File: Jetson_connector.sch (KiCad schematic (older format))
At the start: 18 parts, among them IC2 AT24MAC402-MAHM-T, J2 QTH-060-01-L-D-A, U1 LP5907MFX-1.8

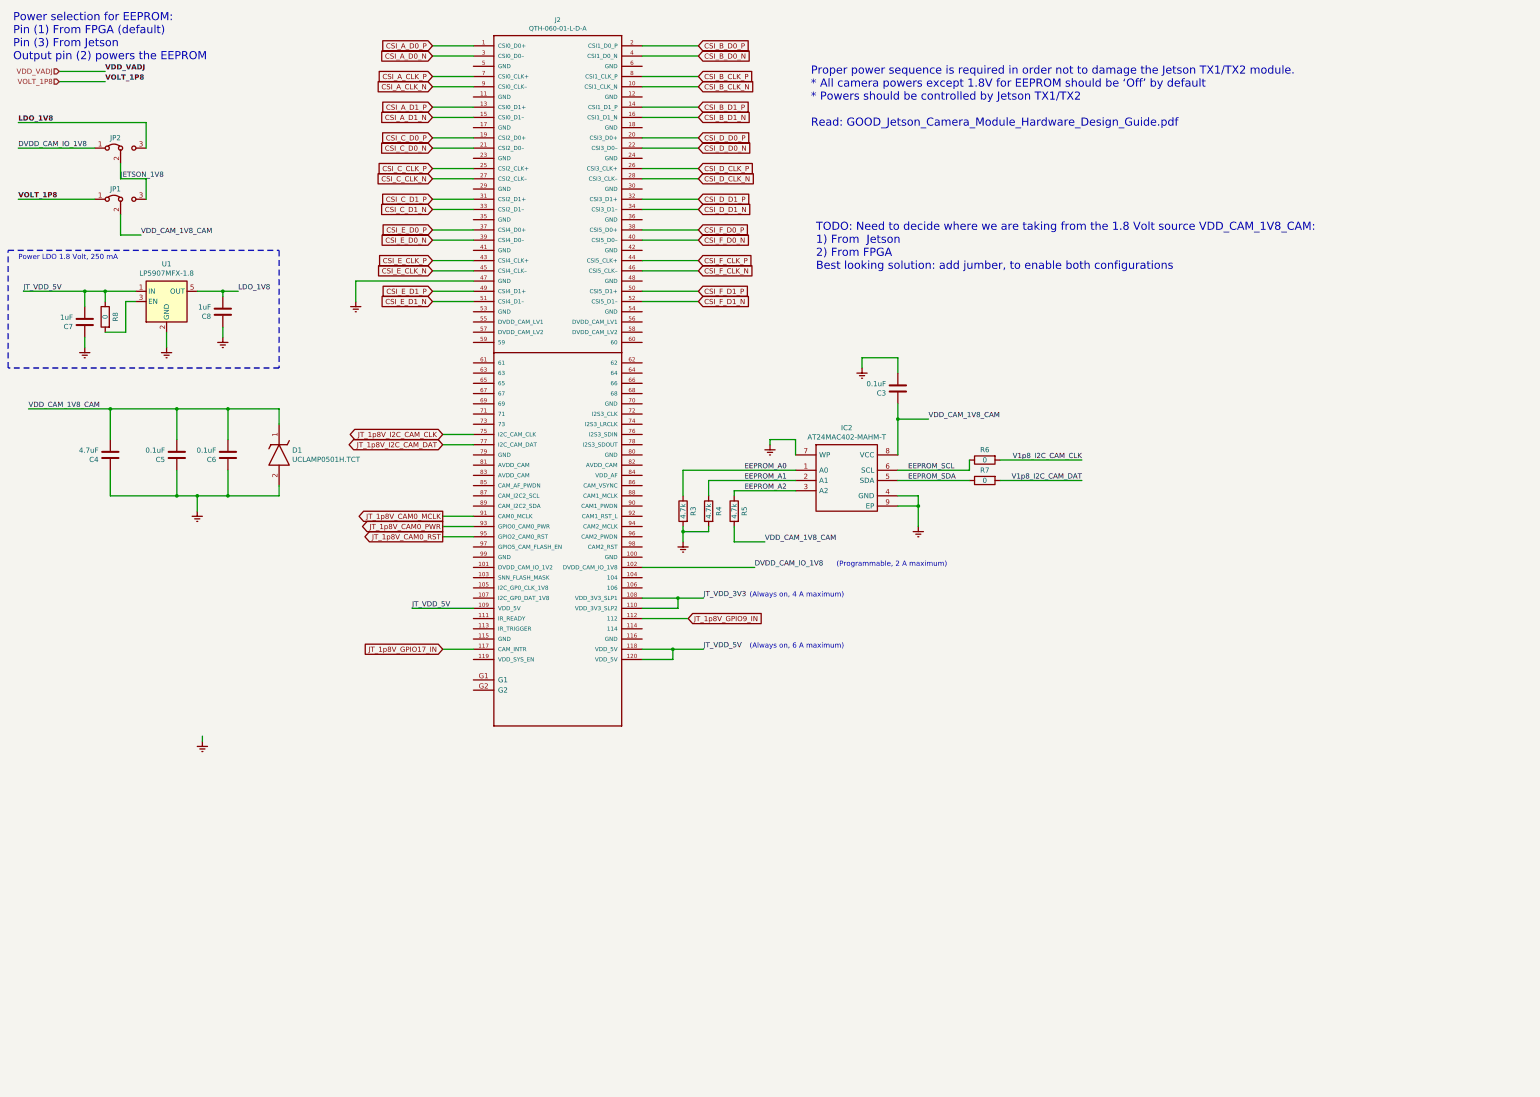
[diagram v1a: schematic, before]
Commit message: adding more power supplies
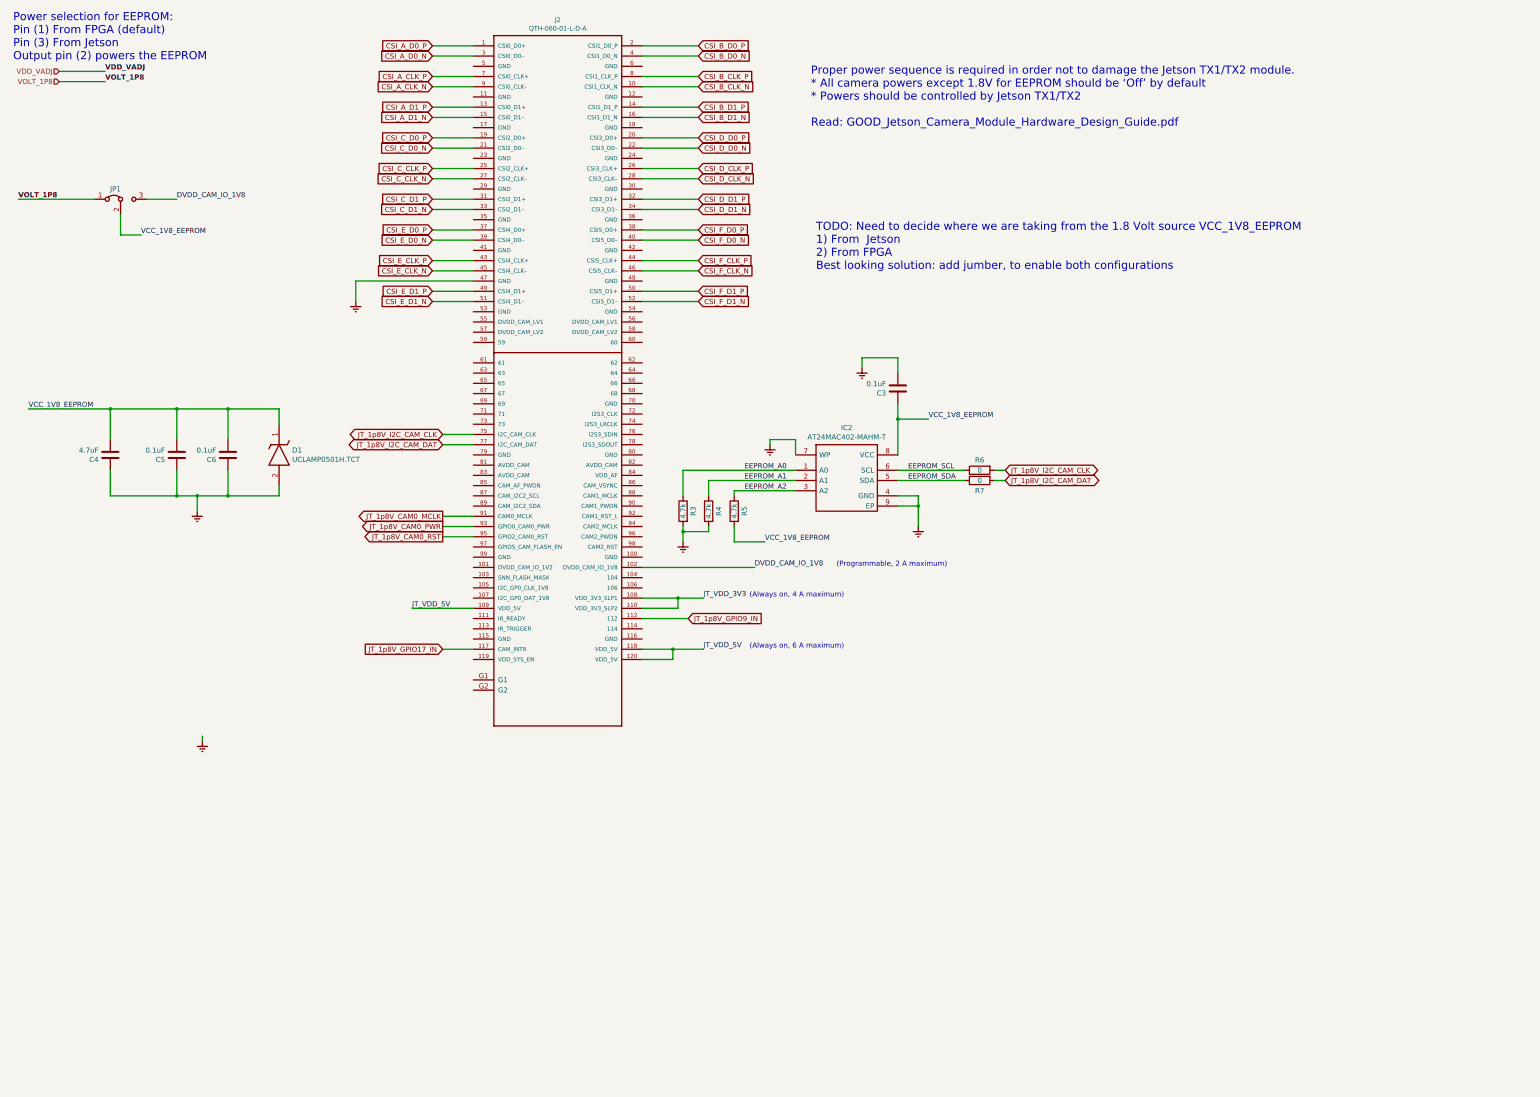
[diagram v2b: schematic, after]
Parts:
- removed C7, C8: 1uF, Capacitors_SMD:C_0805, symbol FMC_MIPI_v2:C
- removed JP2: Jumper_3_Bridged12, Pin_Headers:Pin_Header_Straight_1x03_Pitch2.54mm, symbol Jumper:Jumper_3_Bridged12
- removed R8: 0, Resistors_SMD:R_0805, symbol Device:R
- removed U1: LP5907MFX-1.8, TO_SOT_Packages_SMD:SOT-23-5, symbol Regulator_Linear:LP5907MFX-1.8
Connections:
- net JETSON_1V8 is gone; now on net DVDD_CAM_IO_1V8: JP1.3 (B)
- net V1p8_I2C_CAM_CLK is gone; now on net JT_1p8V_I2C_CAM_CLK: R6.2
- net V1p8_I2C_CAM_DAT is gone; now on net JT_1p8V_I2C_CAM_DAT: R7.2
- net VDD_CAM_1V8_CAM renamed VCC_1V8_EEPROM
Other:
- note added: "TODO: Need to decide where we are taking from the 1.8 Volt source VCC_1V8_EEPROM\n1) From Jetson\n2) From FPGA\nBest looking solution: add jumber, to enable both configurations"
- note removed: "Power LDO 1.8 Volt, 250 mA"
- note removed: "TODO: Need to decide where we are taking from the 1.8 Volt source VDD_CAM_1V8_CAM:\n1) From Jetson\n2) From FPGA\nBest looking solution: add jumber, to enable both configurations"
- moved on the sheet: R6, R7

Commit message: cleanup 3D shapes
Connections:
- net DVDD_CAM_IO_1V8 renamed JT_VDD_1V8
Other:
- moved on the sheet: C3, IC2, R3, R4, R5, R6, R7

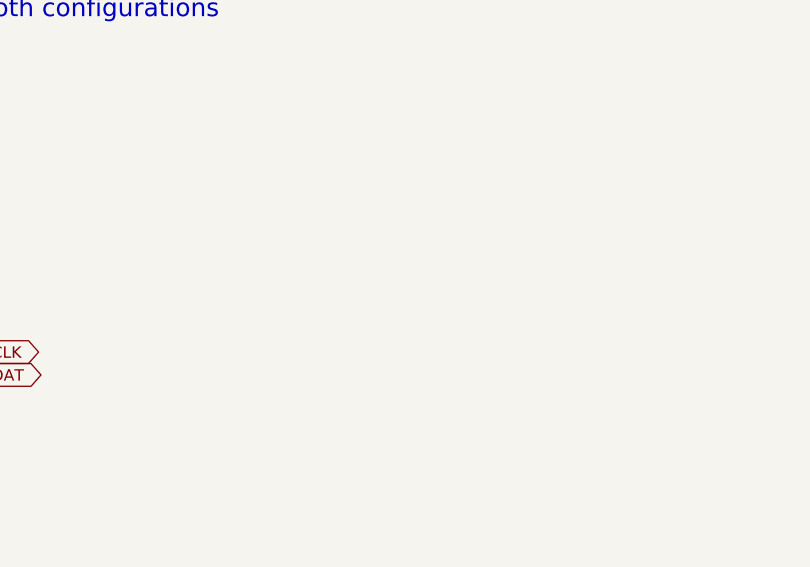
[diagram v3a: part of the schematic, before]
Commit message: Adding more LVDS lines
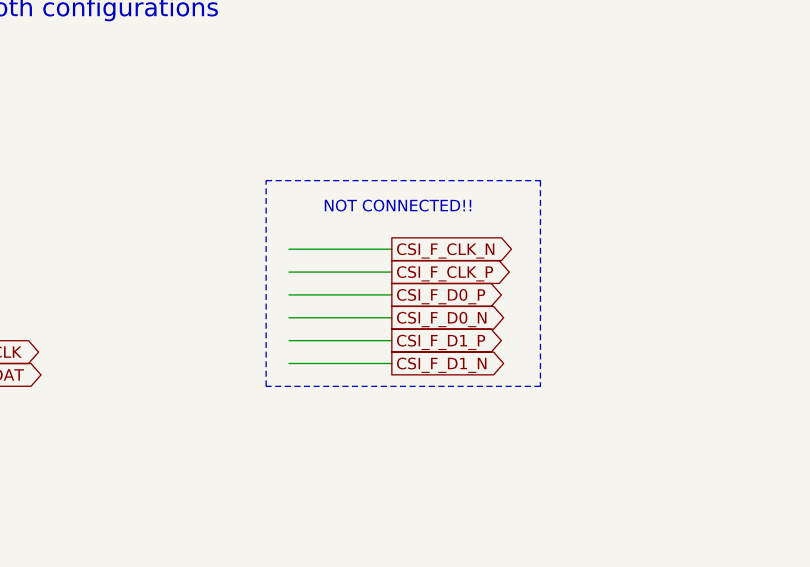
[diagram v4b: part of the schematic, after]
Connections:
- wire segments 108 -> 114
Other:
- note added: "NOT CONNECTED!!"
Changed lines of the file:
@@
 $Descr A4 11693 8268
 encoding utf-8
-Sheet 3 12
+Sheet 3 19
 Title ""
 Date ""
@@
 Text Label 7900 5200 0    50   ~ 0
 VCC_1V8_EEPROM
+Text GLabel 12700 4250 2    50   Output ~ 0
+CSI_F_D0_P
+Text GLabel 12700 4350 2    50   Output ~ 0
+CSI_F_D0_N
+Text GLabel 12700 4150 2    50   Output ~ 0
+CSI_F_CLK_P
+Text GLabel 12700 4050 2    50   Output ~ 0
+CSI_F_CLK_N
+Text GLabel 12700 4450 2    50   Output ~ 0
+CSI_F_D1_P
+Text GLabel 12700 4550 2    50   Output ~ 0
+CSI_F_D1_N
+Wire Wire Line
+	12250 4050 12700 4050
+Wire Wire Line
+	12250 4150 12700 4150
+Wire Wire Line
+	12250 4250 12700 4250
+Wire Wire Line
+	12250 4350 12700 4350
+Wire Wire Line
+	12250 4450 12700 4450
+Wire Wire Line
+	12250 4550 12700 4550
+Text Notes 12400 3900 0    50   ~ 0
+NOT CONNECTED!!
+Wire Notes Line
+	12150 3750 13350 3750
+Wire Notes Line
+	13350 3750 13350 4650
+Wire Notes Line
+	13350 4650 12150 4650
+Wire Notes Line
+	12150 4650 12150 3750
 $EndSCHEMATC

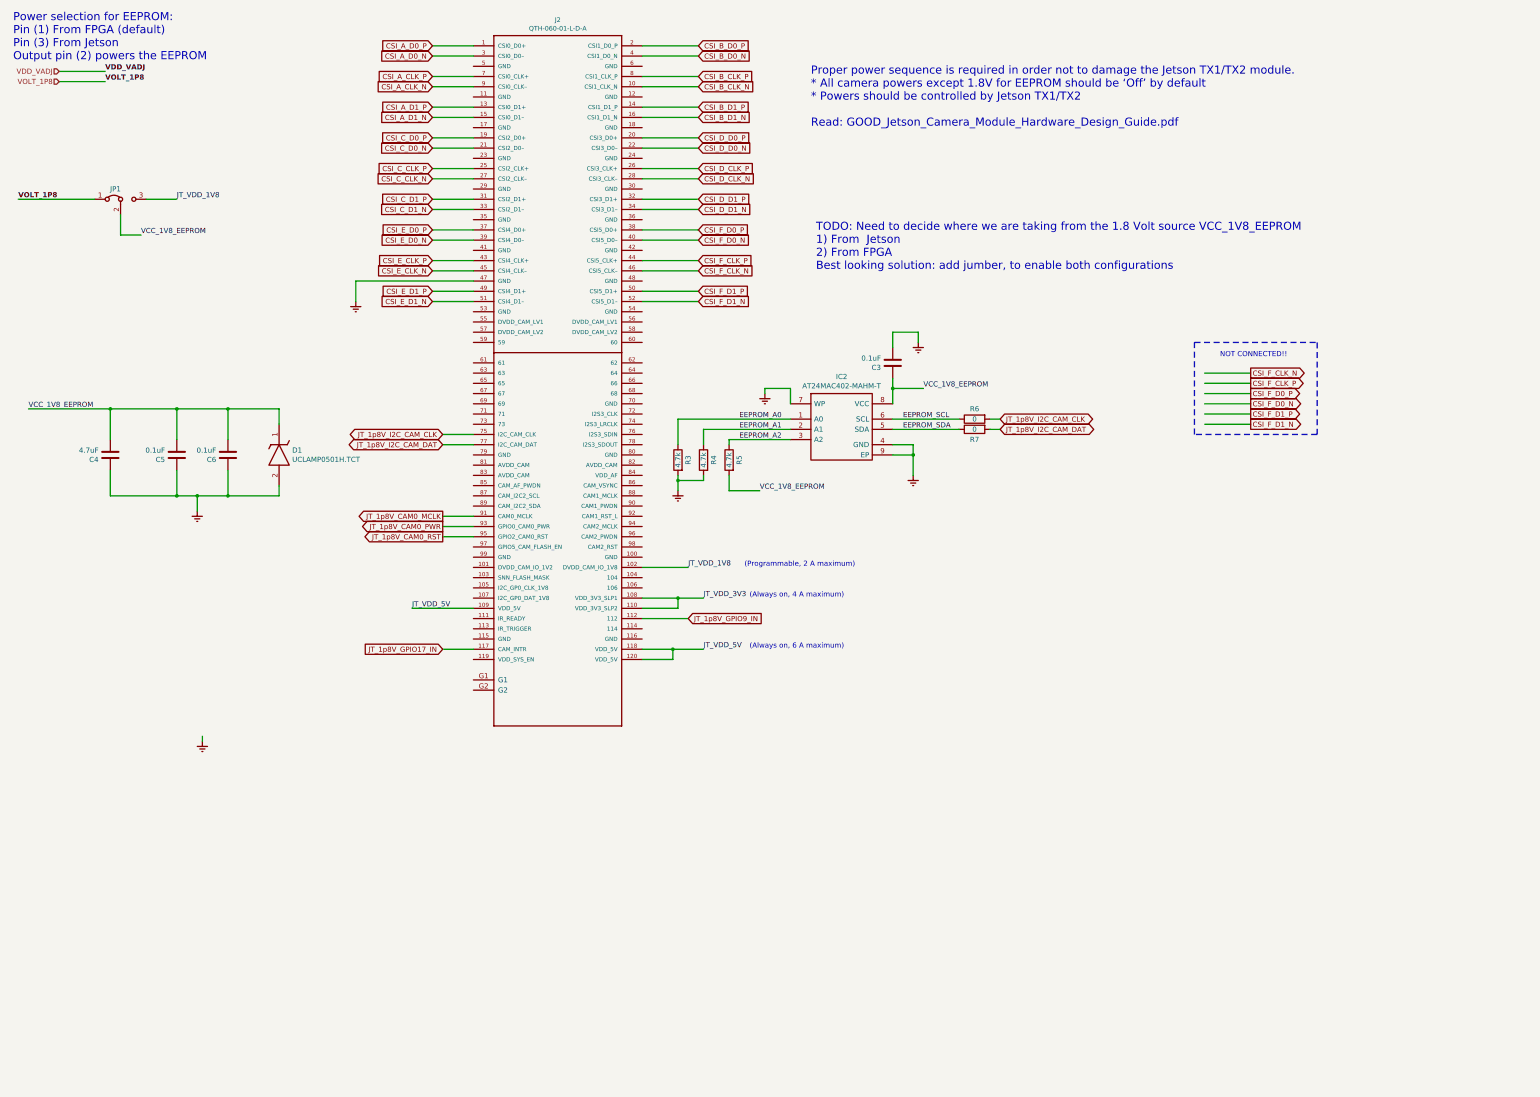
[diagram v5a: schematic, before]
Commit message: added enable line for slow signals
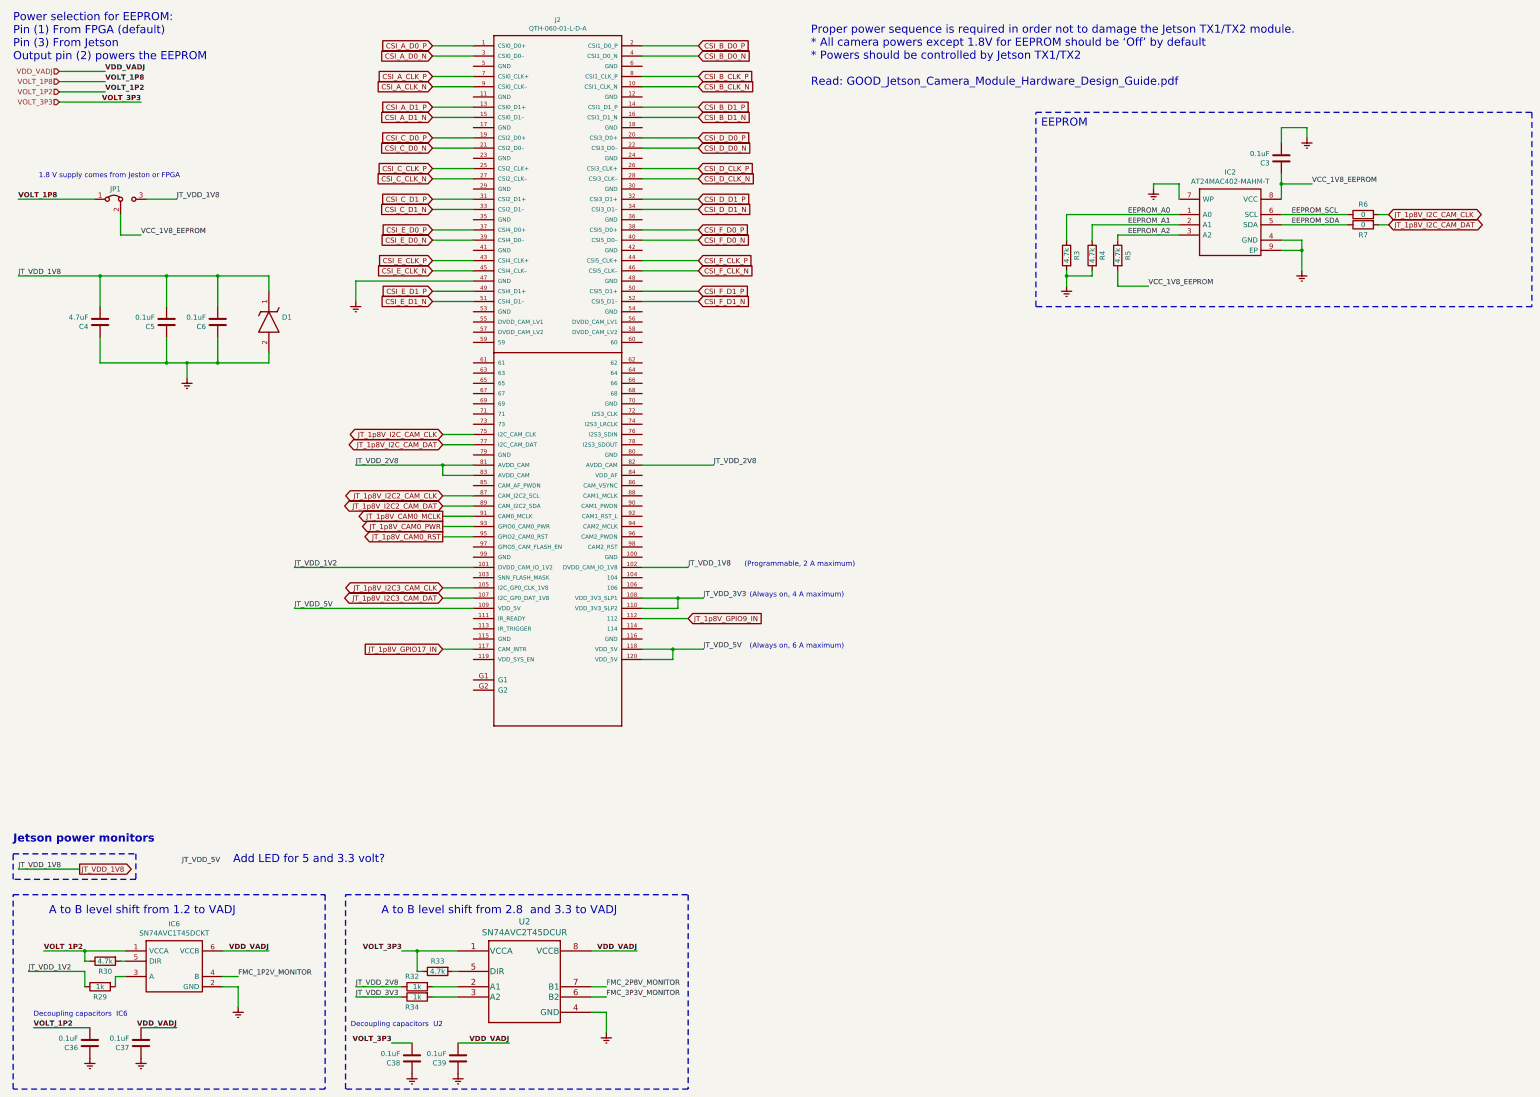
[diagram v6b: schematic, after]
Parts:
- added C36, C37, C38, C39: 0.1uF, Capacitors_SMD:C_0402, symbol FMC_MIPI_v2:C
- added IC6: SN74AVC1T45DCKT, FMC_MIPI_v2_sym:SOT65P210X110-6N, symbol FMC_MIPI_v2:SN74AVC1T45DCKT
- added R29, R32, R34: 1k, Resistors_SMD:R_0805, symbol Device:R
- added R30, R33: 4.7k, Resistors_SMD:R_0805, symbol Device:R
- added U2: SN74AVC2T45DCUR, FMC_MIPI_v2_sym:SN74AVC2T45DCUR, symbol FMC_MIPI_v2:SN74AVC2T45DCUR
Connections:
- net labels added: FMC_1P2V_MONITOR, FMC_2P8V_MONITOR, FMC_3P3V_MONITOR, JT_1p8V_I2C2_CAM_CLK, JT_1p8V_I2C2_CAM_DAT, JT_1p8V_I2C3_CAM_CLK, JT_1p8V_I2C3_CAM_DAT, JT_VDD_1V2, JT_VDD_2V8, VOLT_1P2, VOLT_3P3
- wire segments 114 -> 151
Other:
- note added: "1.8 V supply comes from Jeston or FPGA"
- note added: "A to B level shift from 1.2 to VADJ"
- note added: "A to B level shift from 2.8 and 3.3 to VADJ"
- note added: "Add LED for 5 and 3.3 volt?"
- note added: "Decoupling capacitors IC6"
- note added: "Decoupling capacitors U2"
- note added: "EEPROM"
- note added: "Jetson power monitors"
- note removed: "NOT CONNECTED!!"
- note removed: "TODO: Need to decide where we are taking from the 1.8 Volt source VCC_1V8_EEPROM\n1) From Jetson\n2) From FPGA\nBest looking solution: add jumber, to enable both configurations"
- moved on the sheet: C3, C4, C5, C6, D1, IC2, R3, R4, R5, R6, R7
